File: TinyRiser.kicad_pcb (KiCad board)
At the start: 4 copper layers, 113.2 x 23.5 mm, 32 parts, among them J2 Bus_PCI_Express_x16, J3 Bus_M.2_Socket_M, J4 fancontrol_header, M1 Fan_4pin

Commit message: starting to add smbus to fan control header
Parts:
- added J5: Conn_02x04_Odd_Even, Connector_PinSocket_2.54mm:PinSocket_2x04_P2.54mm_Horizontal, F.Cu at (148.3, 115.6)

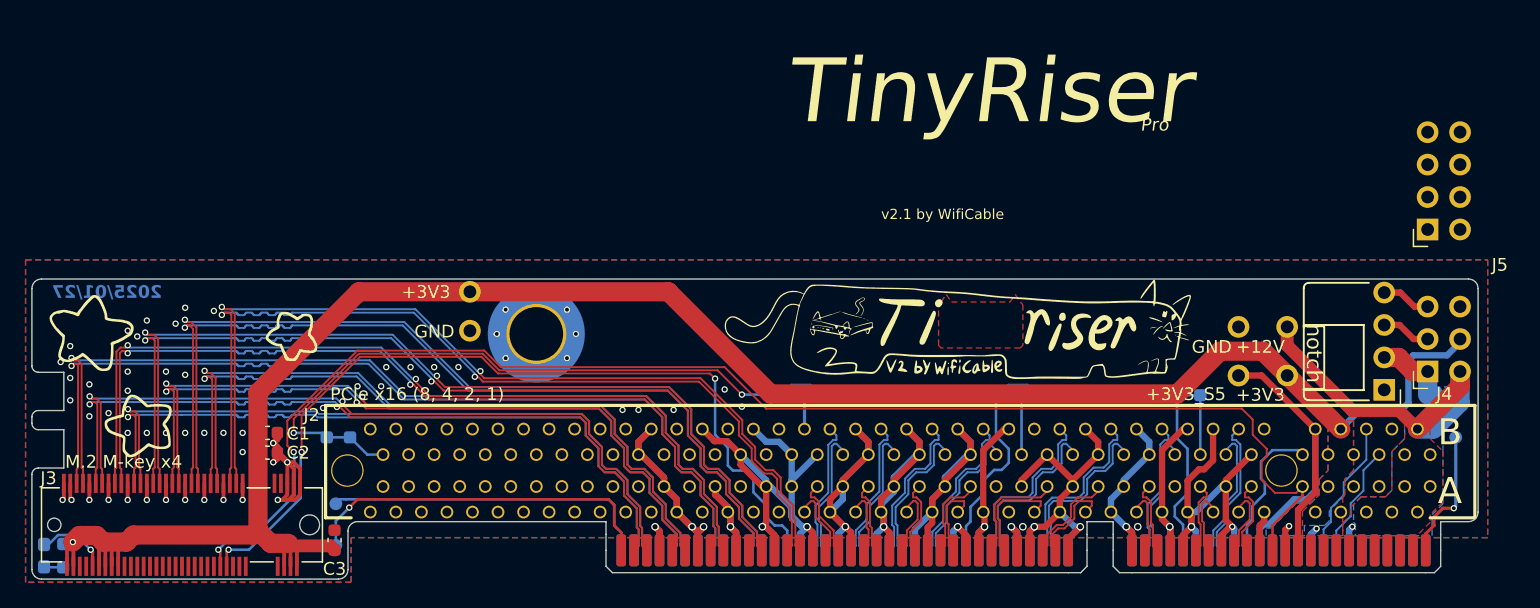
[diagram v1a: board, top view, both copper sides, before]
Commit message: Finished adding smbus to fan control header
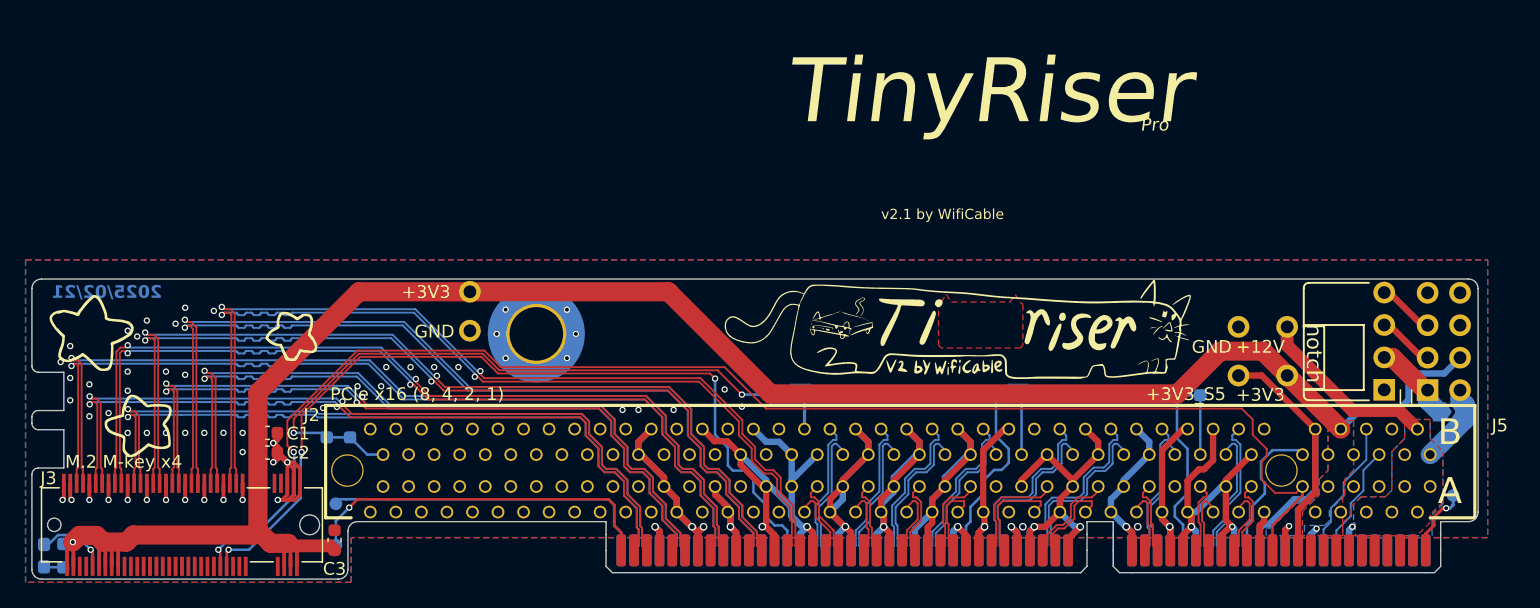
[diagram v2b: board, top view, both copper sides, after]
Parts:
- removed J4: fancontrol_header, Connector_PinSocket_2.54mm:PinSocket_2x03_P2.54mm_Horizontal
- moved J5 12.6 mm to (148.3, 128.2)
- moved TP1 4.55 mm to (150.3, 136.4)
- moved JP1 1.33 mm to (149.9, 129.9)
- moved G*** 1.20 mm to (140.1, 125.5)
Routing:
- net SMBCLK: track 8.89 -> 26.1 mm
- net SMBDATA: track 10.9 -> 24.5 mm
- net +12V: track 26.9 -> 20.7 mm
- net Net-(J1-PCIE_SOLT_A60): track 10.3 -> 5.51 mm
- net +3V3: track 158.5 -> 156.8 mm
- net +12V_fan: track 5.69 -> 6.53 mm
- net PWM_fan: track 3.86 -> 4.46 mm
- net Taco_fan: track 3.86 -> 4.46 mm
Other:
- board text added: "2025/02/21"
- board text added: "Fan 12V bypass"
- board text added: "SMB CLK"
- board text added: "SMB DAT"
- board text removed: "2025/01/27"

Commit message: small silkscreen changes for 12V jumper
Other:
- board text added: "Fan 12V jumper"
- board text removed: "Fan 12V bypass"
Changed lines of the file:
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@@
 			(at -0.025 1.450001 360)
 			(layer "B.SilkS")
+			(hide yes)
 			(effects
 				(font
@@
 	)
 	(gr_line
+		(start 151.35 129.2)
+		(end 151.35 130.6)
+		(stroke
+			(width 0.15)
+			(type default)
+		)
+		(layer "B.SilkS")
+	)
+	(gr_line
 		(start 40.15 141.3)
 		(end 39.95 141)
@@
 	)
 	(gr_line
+		(start 148.5 129.2)
+		(end 148.5 130.6)
+		(stroke
+			(width 0.15)
+			(type default)
+		)
+		(layer "B.SilkS")
+	)
+	(gr_line
 		(start 138.8 122.2)
 		(end 143.6 122.2)
@@
 	)
 	(gr_line
-		(start 147.95 129.9)
-		(end 148.4 129.9)
+		(start 147.65 129.9)
+		(end 148.1 129.9)
 		(stroke
 			(width 0.15)
@@
 		)
 	)
-	(gr_text "Fan 12V bypass"
-		(at 147.75 130.3 0)
+	(gr_text "Fan 12V jumper"
+		(at 147.5 130.3 0)
 		(layer "B.SilkS")
 		(effects

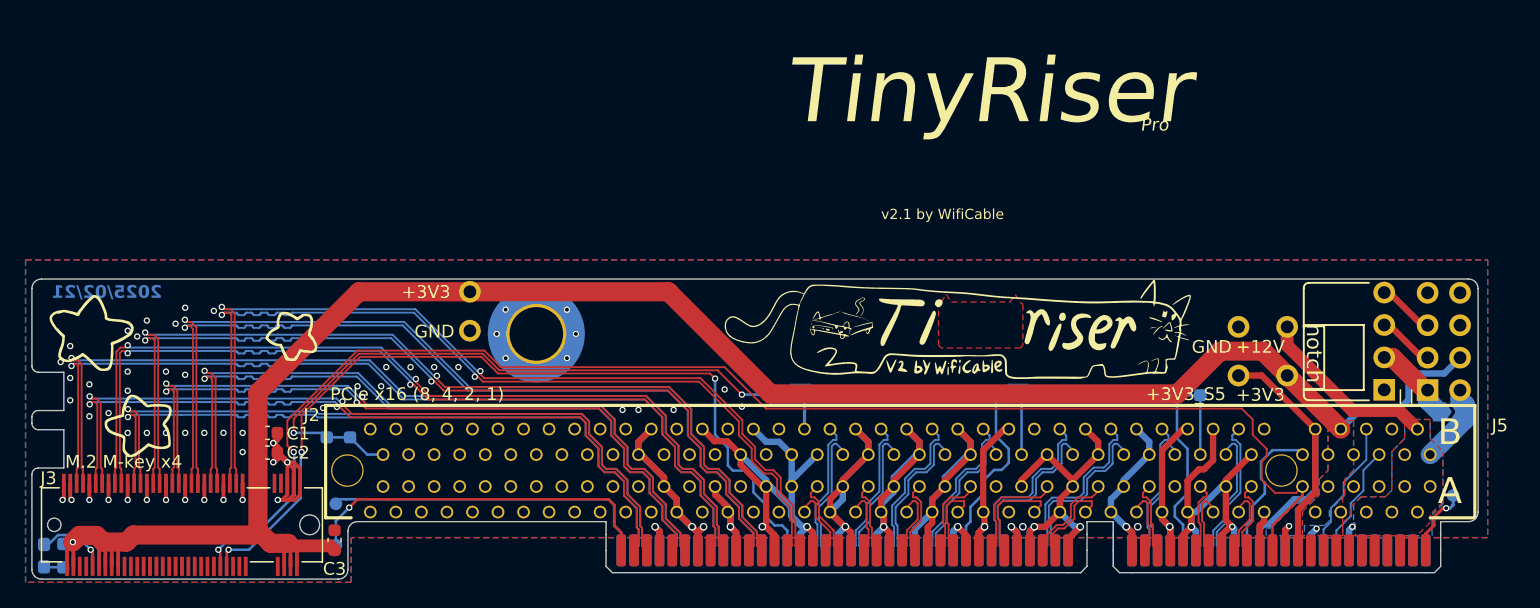
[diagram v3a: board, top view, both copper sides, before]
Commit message: Changed logo to v2.1
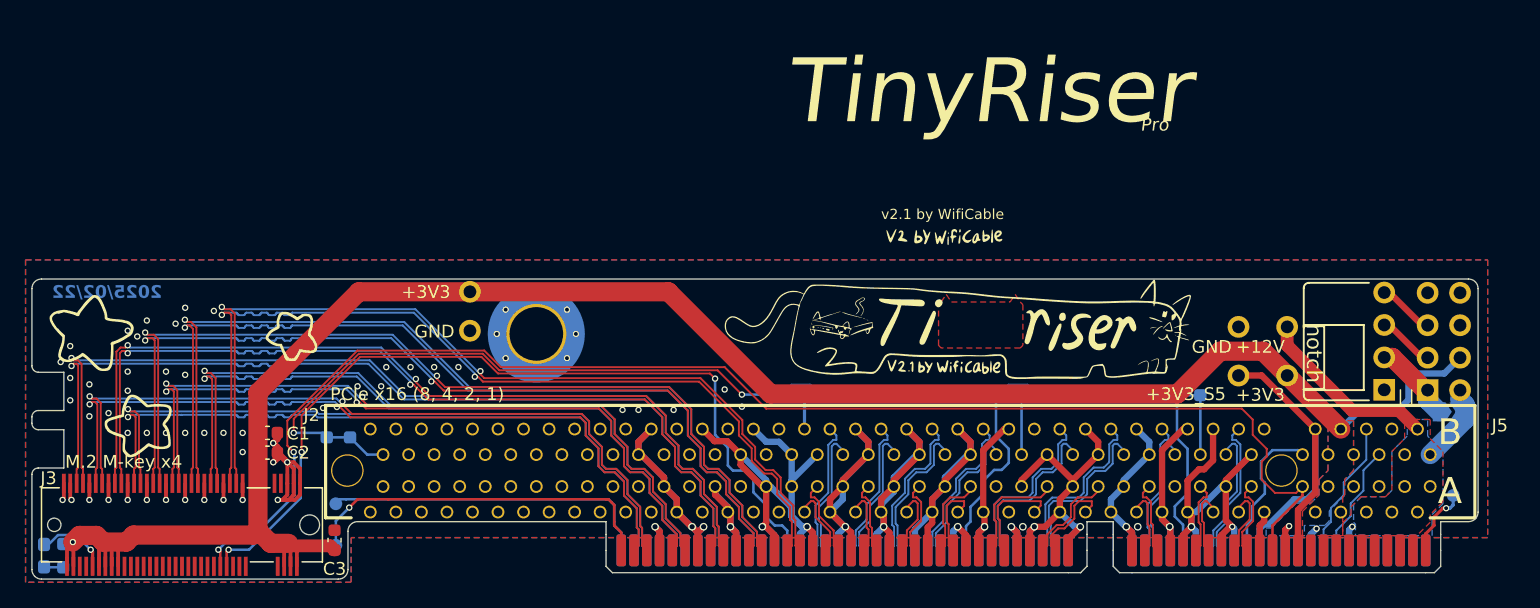
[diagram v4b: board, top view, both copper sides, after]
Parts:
- added G***: LOGO, LOGO, F.Cu at (110.3, 126.3)
- moved G*** 10.2 mm to (110.5, 116.2)
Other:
- board text added: "12V SYS"
- board text added: "2025/02/22"
- board text removed: "12V"
- board text removed: "2025/02/21"
